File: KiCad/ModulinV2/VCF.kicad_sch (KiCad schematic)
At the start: 52 parts, among them IC54 AS3320D, IC55 AS3320D, IC56 TL072HIDR

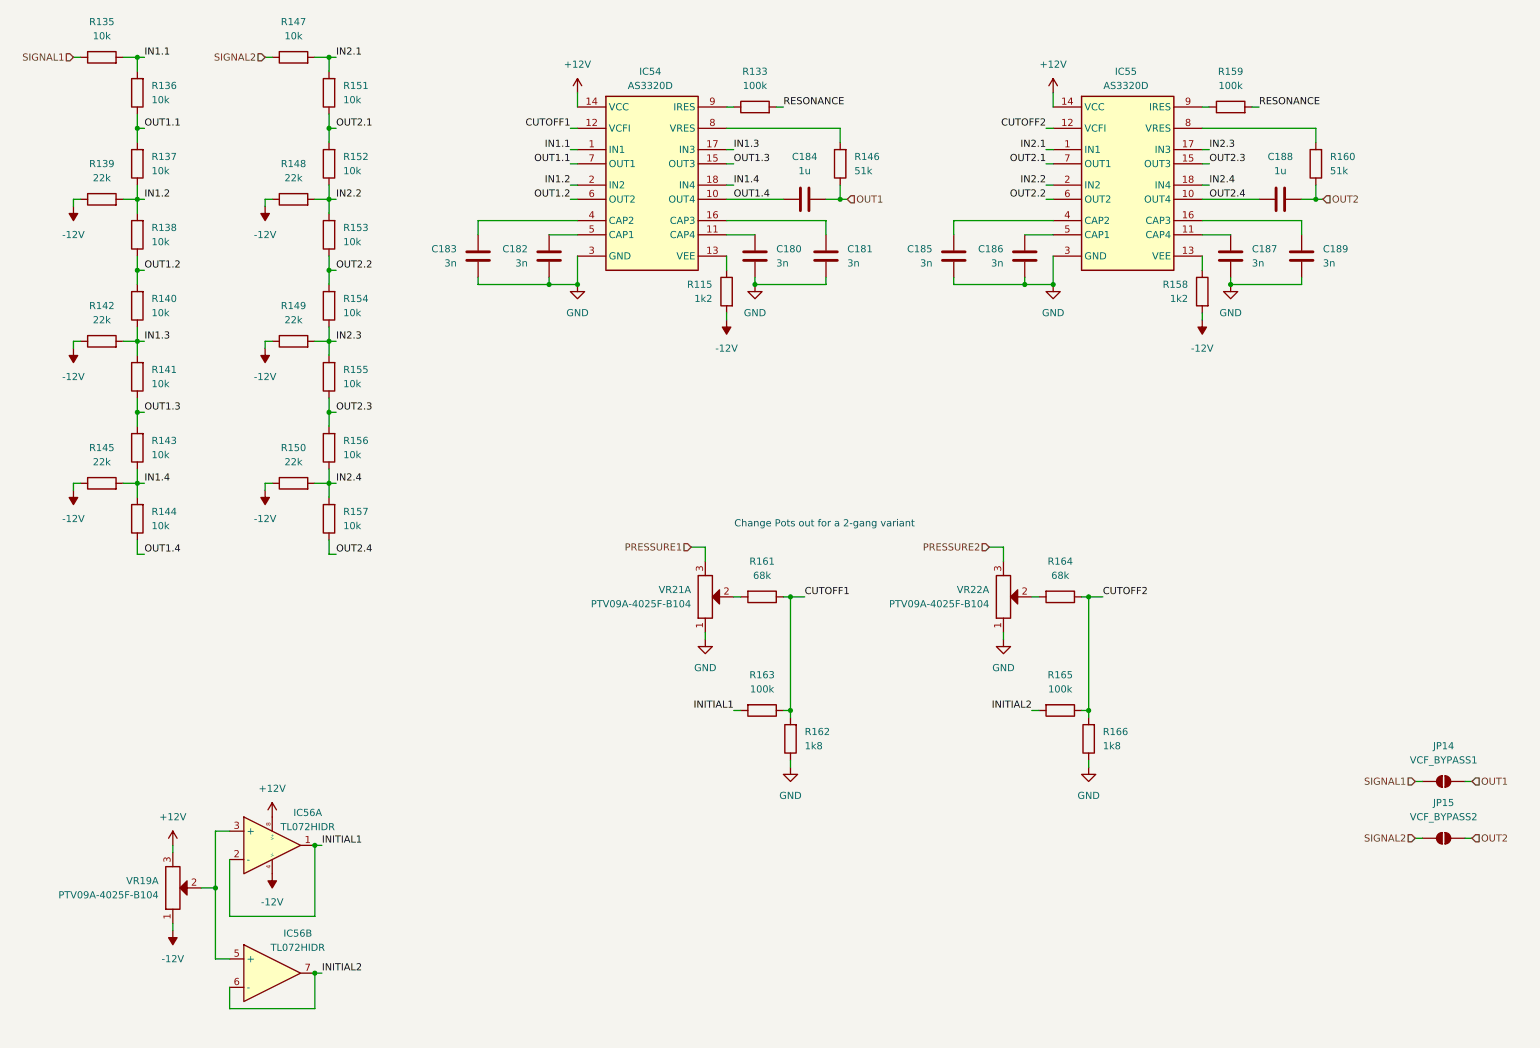
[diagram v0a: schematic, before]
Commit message: Finished Schematic, started on PCB
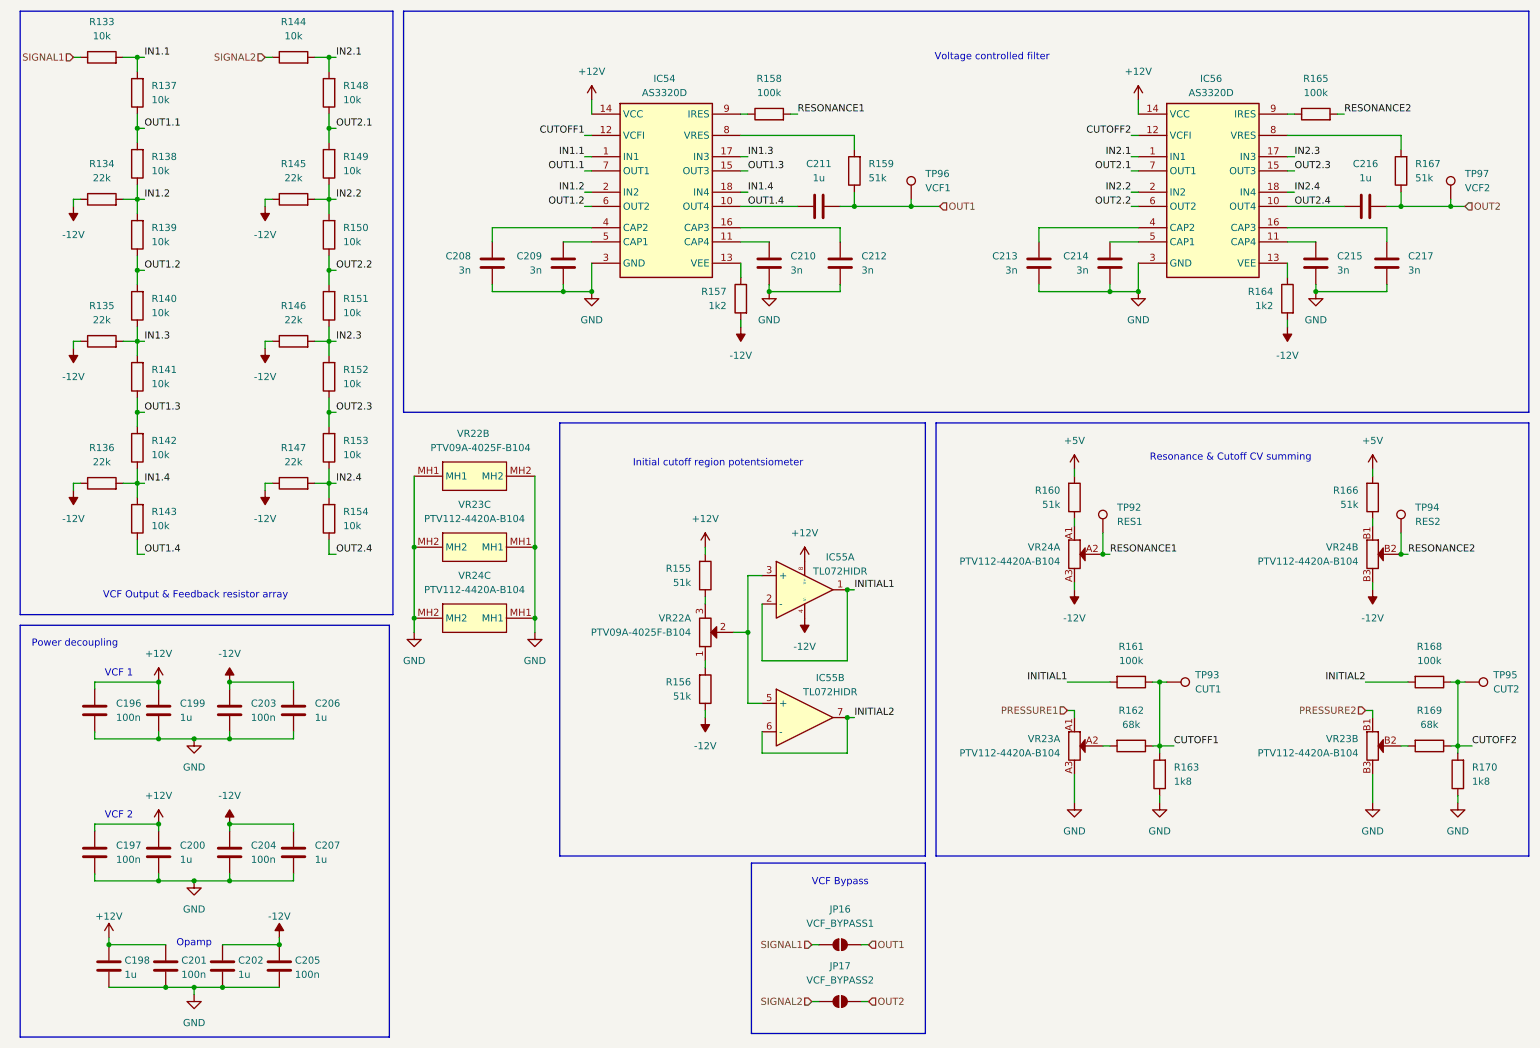
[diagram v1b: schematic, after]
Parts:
- removed VR19, VR21: PTV09A-4025F-B104, SamacSys_Parts:PTV09A4025FB104, symbol SamacSys_Parts:PTV09A-4025F-B104
- added C196, C197, C201, C203, C204, C205: 100n, Capacitor_SMD:C_0603_1608Metric_Pad1.08x0.95mm_HandSolder, symbol Device:C
- added C198, C199, C200, C202, C206, C207: 1u, Capacitor_SMD:C_0603_1608Metric_Pad1.08x0.95mm_HandSolder, symbol Device:C
- added R155, R156, R160, R166: 51k, Resistor_SMD:R_0603_1608Metric_Pad0.98x0.95mm_HandSolder, symbol Device:R
- added TP92: RES1, SamacSys_Parts:TestPointLoop, symbol Connector:TestPoint
- added TP93: CUT1, SamacSys_Parts:TestPointLoop, symbol Connector:TestPoint
- added TP94: RES2, SamacSys_Parts:TestPointLoop, symbol Connector:TestPoint
- added TP95: CUT2, SamacSys_Parts:TestPointLoop, symbol Connector:TestPoint
- added TP96: VCF1, SamacSys_Parts:TestPointLoop, symbol Connector:TestPoint
- added TP97: VCF2, SamacSys_Parts:TestPointLoop, symbol Connector:TestPoint
- added unit 2 of VR22
- added VR23, VR24: PTV112-4420A-B104, SamacSys_Parts:PTV1124420AB104, symbol SamacSys_Parts:PTV112-4420A-B104
- IC54: footprint DIP762W50P254L2300H395Q18N -> Package_SO:SOIC-18W_7.5x11.6mm_P1.27mm
- IC55: renamed from IC56; footprint SOIC127P600X175-8N -> SamacSys_Parts:SOIC127P600X175-8N
- IC56: renamed from IC55; footprint DIP762W50P254L2300H395Q18N -> Package_SO:SOIC-18W_7.5x11.6mm_P1.27mm
- JP16: renamed from JP14; footprint (none) -> Jumper:SolderJumper-2_P1.3mm_Open_TrianglePad1.0x1.5mm
- JP17: renamed from JP15; footprint (none) -> Jumper:SolderJumper-2_P1.3mm_Open_TrianglePad1.0x1.5mm
- R133: renamed from R135; footprint (none) -> Resistor_SMD:R_0603_1608Metric_Pad0.98x0.95mm_HandSolder
- R134: renamed from R139; footprint (none) -> Resistor_SMD:R_0603_1608Metric_Pad0.98x0.95mm_HandSolder
- R135: renamed from R142; footprint (none) -> Resistor_SMD:R_0603_1608Metric_Pad0.98x0.95mm_HandSolder
- R136: renamed from R145; footprint (none) -> Resistor_SMD:R_0603_1608Metric_Pad0.98x0.95mm_HandSolder
- R137: renamed from R136; footprint (none) -> Resistor_SMD:R_0603_1608Metric_Pad0.98x0.95mm_HandSolder
- R138: renamed from R137; footprint (none) -> Resistor_SMD:R_0603_1608Metric_Pad0.98x0.95mm_HandSolder
- R139: renamed from R138; footprint (none) -> Resistor_SMD:R_0603_1608Metric_Pad0.98x0.95mm_HandSolder
- R140, R141: footprint (none) -> Resistor_SMD:R_0603_1608Metric_Pad0.98x0.95mm_HandSolder
- R142: renamed from R143; footprint (none) -> Resistor_SMD:R_0603_1608Metric_Pad0.98x0.95mm_HandSolder
- R143: renamed from R144; footprint (none) -> Resistor_SMD:R_0603_1608Metric_Pad0.98x0.95mm_HandSolder
- R144: renamed from R147; footprint (none) -> Resistor_SMD:R_0603_1608Metric_Pad0.98x0.95mm_HandSolder
- R145: renamed from R148; footprint (none) -> Resistor_SMD:R_0603_1608Metric_Pad0.98x0.95mm_HandSolder
- R146: renamed from R149; footprint (none) -> Resistor_SMD:R_0603_1608Metric_Pad0.98x0.95mm_HandSolder
- R147: renamed from R150; footprint (none) -> Resistor_SMD:R_0603_1608Metric_Pad0.98x0.95mm_HandSolder
- R148: renamed from R151; footprint (none) -> Resistor_SMD:R_0603_1608Metric_Pad0.98x0.95mm_HandSolder
- R149: renamed from R152; footprint (none) -> Resistor_SMD:R_0603_1608Metric_Pad0.98x0.95mm_HandSolder
- R150: renamed from R153; footprint (none) -> Resistor_SMD:R_0603_1608Metric_Pad0.98x0.95mm_HandSolder
- R151: renamed from R154; footprint (none) -> Resistor_SMD:R_0603_1608Metric_Pad0.98x0.95mm_HandSolder
- R152: renamed from R155; footprint (none) -> Resistor_SMD:R_0603_1608Metric_Pad0.98x0.95mm_HandSolder
- R153: renamed from R156; footprint (none) -> Resistor_SMD:R_0603_1608Metric_Pad0.98x0.95mm_HandSolder
- R154: renamed from R157; footprint (none) -> Resistor_SMD:R_0603_1608Metric_Pad0.98x0.95mm_HandSolder
- R157: renamed from R115; footprint (none) -> Resistor_SMD:R_0805_2012Metric_Pad1.20x1.40mm_HandSolder
- R158: renamed from R133; footprint (none) -> Resistor_SMD:R_1206_3216Metric_Pad1.30x1.75mm_HandSolder
- R159: renamed from R146; footprint (none) -> Resistor_SMD:R_0603_1608Metric_Pad0.98x0.95mm_HandSolder
- R161: renamed from R163; footprint (none) -> Resistor_SMD:R_1206_3216Metric_Pad1.30x1.75mm_HandSolder
- R162: renamed from R161; footprint (none) -> Resistor_SMD:R_0603_1608Metric_Pad0.98x0.95mm_HandSolder
- R163: renamed from R162; footprint (none) -> Resistor_SMD:R_1206_3216Metric_Pad1.30x1.75mm_HandSolder
- R164: renamed from R158; footprint (none) -> Resistor_SMD:R_0805_2012Metric_Pad1.20x1.40mm_HandSolder
- R165: renamed from R159; footprint (none) -> Resistor_SMD:R_1206_3216Metric_Pad1.30x1.75mm_HandSolder
- R167: renamed from R160; footprint (none) -> Resistor_SMD:R_0603_1608Metric_Pad0.98x0.95mm_HandSolder
- R168: renamed from R165; footprint (none) -> Resistor_SMD:R_1206_3216Metric_Pad1.30x1.75mm_HandSolder
- R169: renamed from R164; footprint (none) -> Resistor_SMD:R_0603_1608Metric_Pad0.98x0.95mm_HandSolder
- R170: renamed from R166; footprint (none) -> Resistor_SMD:R_1206_3216Metric_Pad1.30x1.75mm_HandSolder
- renumbered C183 to C208, C182 to C209, C180 to C210, C184 to C211, C181 to C212, C185 to C213, C186 to C214, C187 to C215, C188 to C216, C189 to C217
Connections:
- net +12V: now also C196.2, C197.2, C198.1, C199.2, C200.2, C201.1, R155.2
- net -12V: now also C202.1, C203.2, C204.2, C205.1, C206.2, C207.2, R156.1, VR24.A3, VR24.B3
- net CUTOFF1: now also TP93.1
- net CUTOFF2: now also TP95.1
- net GND: now also C196.1, C197.1, C198.2, C199.1, C200.1, C201.2, C202.2, C203.1, C204.1, C205.2, C206.1, C207.1, VR22.MH1, VR22.MH2, VR23.A3, VR23.B3, VR23.MH1, VR23.MH2, VR24.MH1, VR24.MH2; no longer VR22.1
- net OUT1: now also TP96.1
- net OUT2: now also TP97.1
- net PRESSURE1: now also VR23.A1
- net PRESSURE2: now also VR23.B1; no longer VR22.3
- net at R162.2: now also VR23.A2
- net at R169.2: now also VR23.B2; no longer VR22.2
- net at IC55.3 (+), IC55.5 (+): now also VR22.2
- net RESONANCE renamed RESONANCE1
- net RESONANCE1: now also TP92.1, VR24.A2; no longer R165.2
- new net: R156.2, VR22.1
- new net: R166.1, VR24.B1
- new net: R155.1, VR22.3
- new net: R160.1, VR24.A1
- new net +5V: R160.2, R166.2
- new net RESONANCE2: R165.2, TP94.1, VR24.B2
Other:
- note added: "Initial cutoff region potentsiometer"
- note added: "Opamp"
- note added: "Power decoupling"
- note added: "Resonance & Cutoff CV summing"
- note added: "VCF 1"
- note added: "VCF 2"
- note added: "VCF Bypass"
- note added: "VCF Output & Feedback resistor array"
- note added: "Voltage controlled filter"
- note removed: "Change Pots out for a 2-gang variant"
- moved on the sheet: C208, C209, C210, C211, C212, C213, C214, C215, C216, C217, IC54, IC55A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

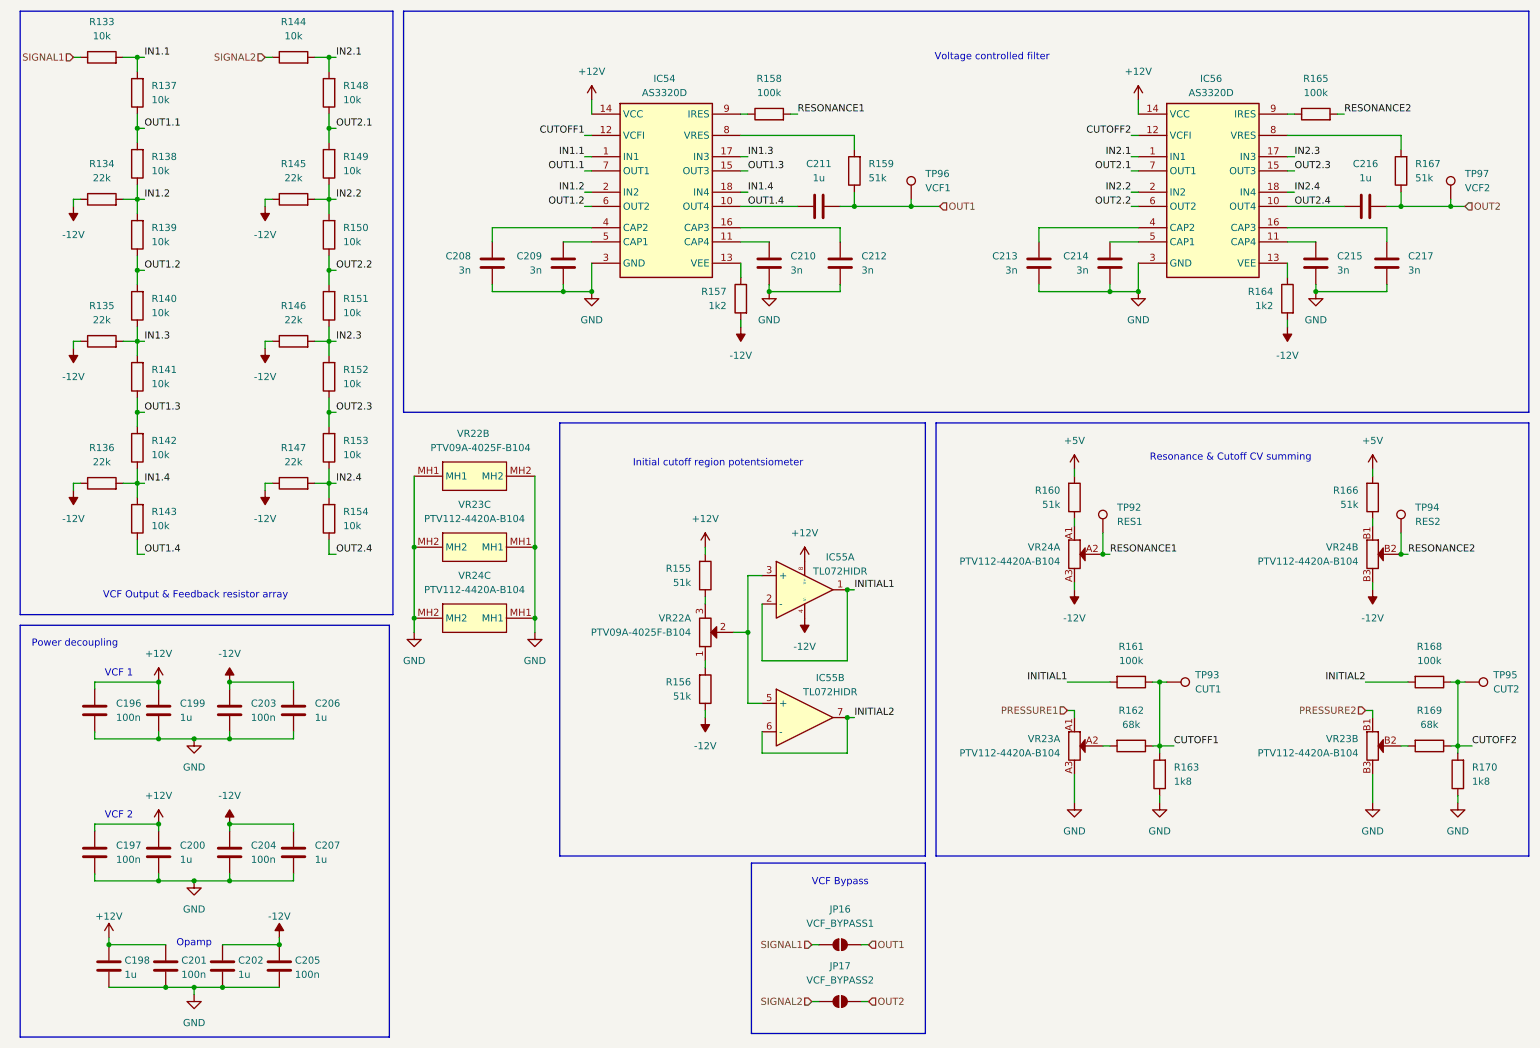
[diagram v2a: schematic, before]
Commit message: Layed out Interface and PWR components and started with MCU layout
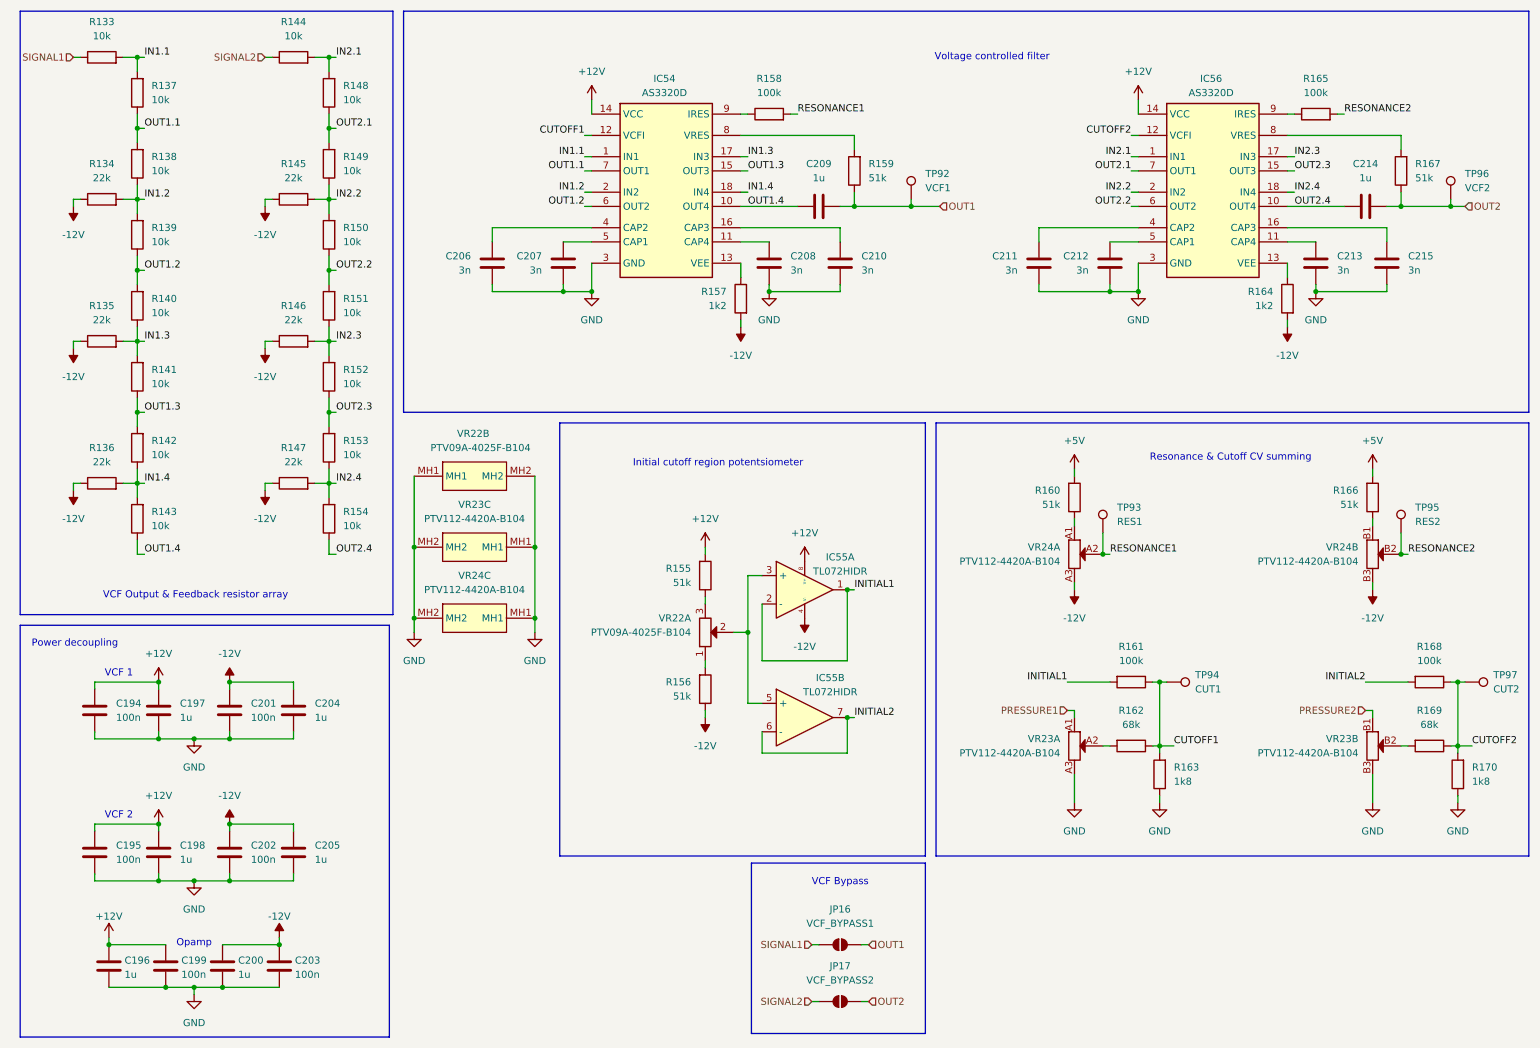
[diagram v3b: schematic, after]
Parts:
- renumbered C196 to C194, C197 to C195, C198 to C196, C199 to C197, C200 to C198, C201 to C199, C202 to C200, C203 to C201, C204 to C202, C205 to C203, C206 to C204, C207 to C205, C208 to C206, C209 to C207, C210 to C208, C211 to C209, C212 to C210, C213 to C211, C214 to C212, C215 to C213, C216 to C214, C217 to C215, TP96 to TP92, TP92 to TP93, TP93 to TP94, TP94 to TP95, TP97 to TP96, TP95 to TP97
